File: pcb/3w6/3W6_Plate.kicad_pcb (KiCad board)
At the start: 2 copper layers, 243.2 x 106 mm, 47 parts

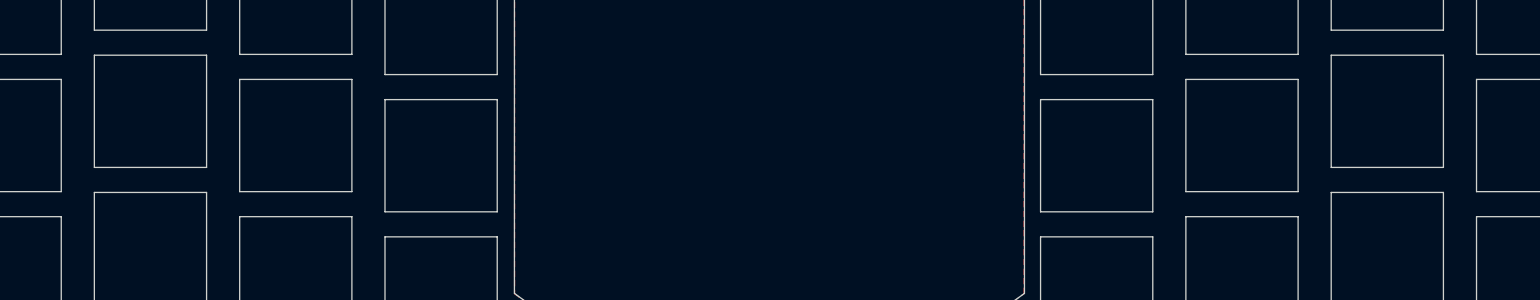
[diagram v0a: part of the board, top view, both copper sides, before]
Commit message: Adding holes for Tenting Puck to Top Plate
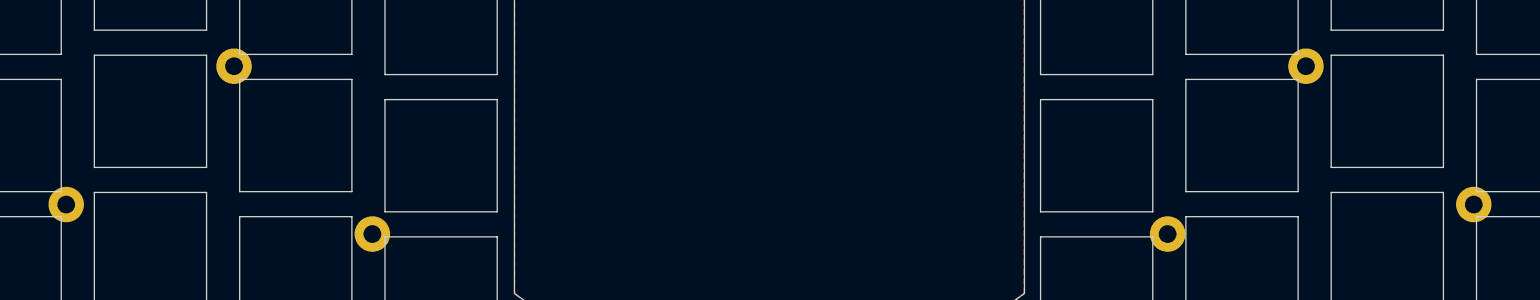
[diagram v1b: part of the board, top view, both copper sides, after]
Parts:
- added REF**: Tenting Puck, Weteor:Tenting_Puck_3hole_nomask, F.Cu at (232.2, 65.7)
- added REF**: Tenting Puck, Weteor:Tenting_Puck_3hole, F.Cu at (95.8, 65.7)
